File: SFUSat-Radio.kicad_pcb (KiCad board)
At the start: 4 copper layers, 95.9 x 90.2 mm, 282 parts, among them J1 PC104-8BIT, J10 TP_TH_150, J11 TP_TH_150, J12 SMA, J13 SMA, J14 SMA, J15 Conn_01x02, J16 SMA, J17 SMA, J18 SMA, J2 PC104PTH, J21 TP_TH_150, J22 TP_TH_150, J23 TP_TH_150, J24 TP_TH_150, J25 Conn_01x02, J3 PC104PTH, J4 PC104PTH, J400 SMA, J401 TP_TH_150, J402 TP_TH_150, J404 TP_TH_150, J405 TP_TH_150, J406 TP_TH_150, J5 PC104PTH, J500 SMA, J501 TP_TH_150, J502 TP_TH_150, J504 TP_TH_150, J505 TP_TH_150, J506 TP_TH_150, J6 SMA, J7 TP_TH_150, J8 TP_TH_150, J9 TP_TH_150, P1 3pin-DC-power, U1 SINGLE_0402, U10 TPS799, U100 CC1101-Q1, U101 0433BM15A0001, U11 SINGLE_0402, U110 CC1101-Q1, U111 0915BM15A0001E, U12 CONN_02X05_SHRD, U13 CONN_02X05_SHRD, U14 2N7002DW, U15 TPS62175DQCR, U16 TPS71750DSER, U17 74LVC1G14SE-7, U2 SKY13345-368LF, U3 CD4555BPWR, U4 LMS3635AQRNLRQ1, U400 SINGLE_0402, U401 LMV358, U402 RF6886, U420 2N7002DW, U5 MML09211H, U500 SINGLE_0402, U501 LMV358, U502 RF6886, U6 SINGLE_0402, U600 STLM75, U610 STLM75, U7 SKY13372-467LF, U8 SINGLE_0402, U9 TLV702, X100 NX3225GA, X110 NX3225GA

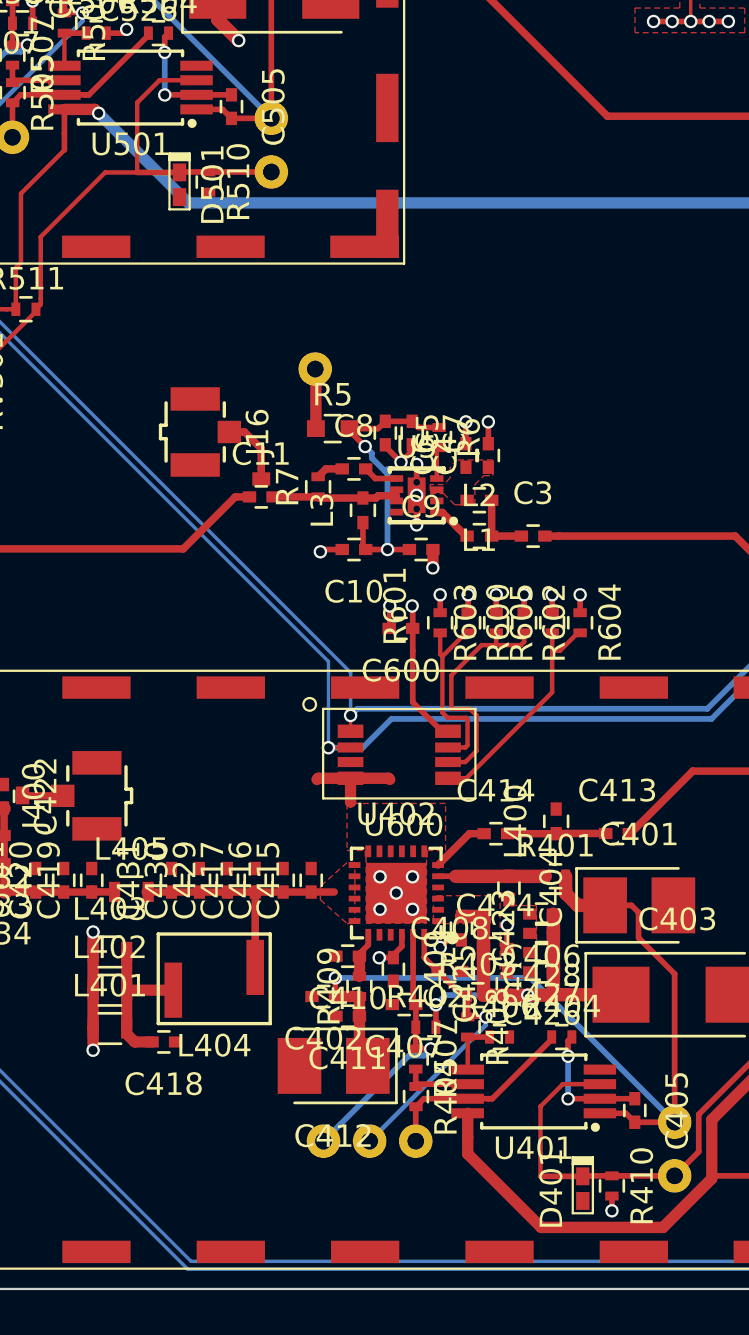
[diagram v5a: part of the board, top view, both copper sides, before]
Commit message: modified proposed pot schematic
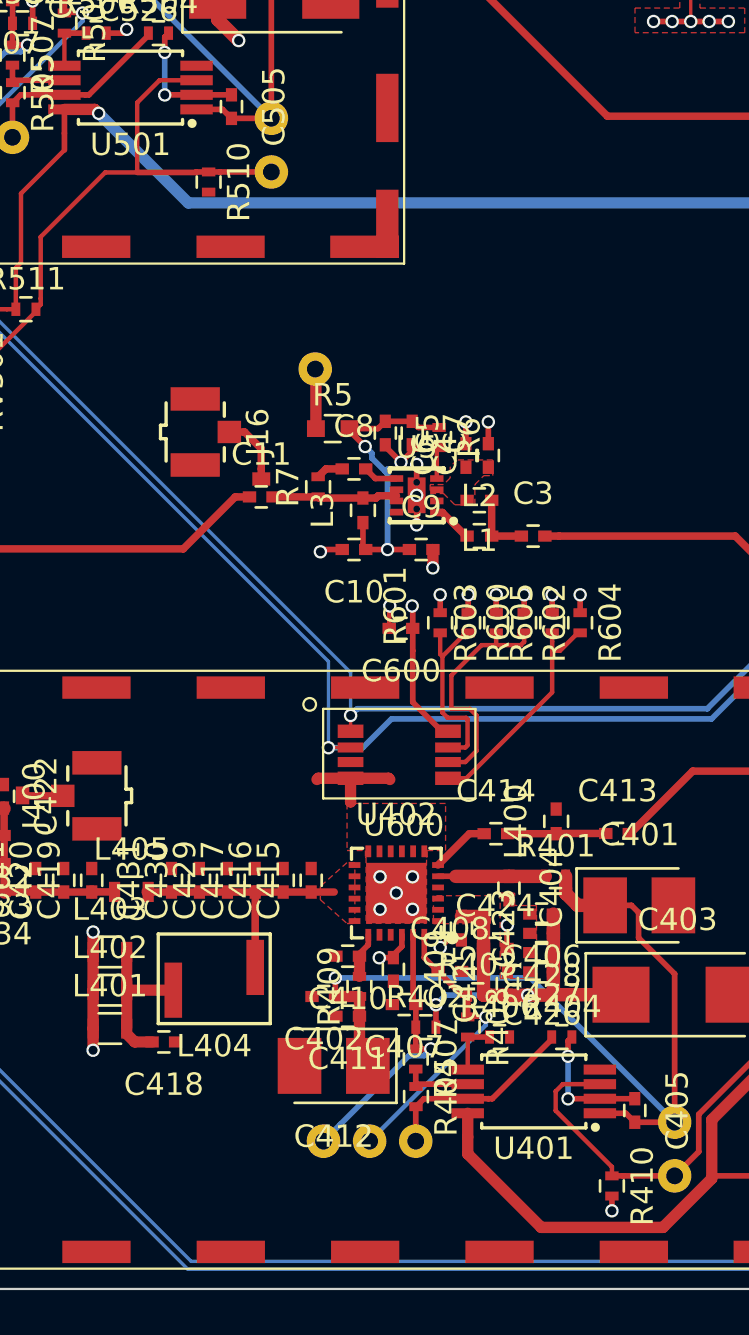
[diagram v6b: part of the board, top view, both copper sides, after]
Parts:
- removed D401, D501: PESD5Zx, SFUSat:PESD57zx
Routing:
- net /PA_LB/GAIN: track 37.8 -> 35.3 mm
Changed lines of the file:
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@@
     (thickness 1.6)
     (drawings 26)
-    (tracks 1615)
+    (tracks 1613)
     (zones 0)
-    (modules 282)
+    (modules 280)
     (nets 205)
   )
@@
       (net 1 GND))
   )
-  (module SFUSat:PESD57zx (layer F.Cu)
-    (at 142.86 99.19 270)
-    (fp_text reference D501 (at 0 -1.5 270) (layer F.SilkS)
-      (effects (font (size 1 1) (thickness 0.15)))
-    )
-    (fp_text value PESD5Zx (at 0 1.5 270) (layer F.Fab)
-      (effects (font (size 1 1) (thickness 0.15)))
-    )
-    (fp_line (start -1.6 -0.65) (end 1.3 -0.65) (layer F.CrtYd) (width 0.1))
-    (fp_line (start 1.3 -0.65) (end 1.3 0.65) (layer F.CrtYd) (width 0.1))
-    (fp_line (start 1.3 0.65) (end -1.6 0.65) (layer F.CrtYd) (width 0.1))
-    (fp_line (start -1.6 0.65) (end -1.6 -0.65) (layer F.CrtYd) (width 0.1))
-    (fp_text user REF** (at 0 -1.5 270) (layer F.Fab)
-      (effects (font (size 1 1) (thickness 0.15)))
-    )
-    (fp_line (start -1.4 -0.45) (end -1.4 0.45) (layer F.SilkS) (width 0.1))
-    (fp_line (start -1.2 -0.45) (end -1.2 0.45) (layer F.SilkS) (width 0.1))
-    (fp_line (start -1.1 -0.45) (end -1.4 -0.45) (layer F.SilkS) (width 0.1))
-    (fp_line (start -1.3 -0.45) (end -1.3 0.45) (layer F.SilkS) (width 0.1))
-    (fp_line (start -1.4 0.45) (end -1.1 0.45) (layer F.SilkS) (width 0.1))
-    (fp_line (start -1.1 -0.45) (end 1.1 -0.45) (layer F.SilkS) (width 0.1))
-    (fp_line (start 1.1 -0.45) (end 1.1 0.45) (layer F.SilkS) (width 0.1))
-    (fp_line (start 1.1 0.45) (end -1.1 0.45) (layer F.SilkS) (width 0.1))
-    (fp_line (start -1.1 0.45) (end -1.1 -0.45) (layer F.SilkS) (width 0.1))
-    (fp_line (start -0.15 0.225) (end -0.05 0.225) (layer F.Fab) (width 0.1))
-    (fp_line (start -1 -0.35) (end 1 -0.35) (layer F.Fab) (width 0.1))
-    (fp_line (start 1 -0.35) (end 1 0.35) (layer F.Fab) (width 0.1))
-    (fp_line (start 1 0.35) (end -1 0.35) (layer F.Fab) (width 0.1))
-    (fp_line (start -1 0.35) (end -1 -0.35) (layer F.Fab) (width 0.1))
-    (fp_line (start -0.15 -0.225) (end -0.15 0.225) (layer F.Fab) (width 0.1))
-    (fp_line (start 0.125 -0.225) (end 0.125 0.225) (layer F.Fab) (width 0.1))
-    (fp_line (start 0.125 0.225) (end -0.1 0) (layer F.Fab) (width 0.1))
-    (fp_line (start -0.1 0) (end 0.125 -0.225) (layer F.Fab) (width 0.1))
-    (pad 1 smd rect (at -0.55 0 270) (size 0.8 0.6) (layers F.Cu F.Paste F.Mask)
-      (net 106 /PA_UB/GAIN))
-    (pad 2 smd rect (at 0.55 0 270) (size 0.8 0.6) (layers F.Cu F.Paste F.Mask)
-      (net 1 GND))
-  )
-  (module SFUSat:PESD57zx (layer F.Cu)
-    (at 160.87 144.02 270)
-    (fp_text reference D401 (at 0 1.39 270) (layer F.SilkS)
-      (effects (font (size 1 1) (thickness 0.15)))
-    )
-    (fp_text value PESD5Zx (at 0 1.5 270) (layer F.Fab)
-      (effects (font (size 1 1) (thickness 0.15)))
-    )
-    (fp_line (start -1.6 -0.65) (end 1.3 -0.65) (layer F.CrtYd) (width 0.1))
-    (fp_line (start 1.3 -0.65) (end 1.3 0.65) (layer F.CrtYd) (width 0.1))
-    (fp_line (start 1.3 0.65) (end -1.6 0.65) (layer F.CrtYd) (width 0.1))
-    (fp_line (start -1.6 0.65) (end -1.6 -0.65) (layer F.CrtYd) (width 0.1))
-    (fp_text user REF** (at 0 -1.5 270) (layer F.Fab)
-      (effects (font (size 1 1) (thickness 0.15)))
-    )
-    (fp_line (start -1.4 -0.45) (end -1.4 0.45) (layer F.SilkS) (width 0.1))
-    (fp_line (start -1.2 -0.45) (end -1.2 0.45) (layer F.SilkS) (width 0.1))
-    (fp_line (start -1.1 -0.45) (end -1.4 -0.45) (layer F.SilkS) (width 0.1))
-    (fp_line (start -1.3 -0.45) (end -1.3 0.45) (layer F.SilkS) (width 0.1))
-    (fp_line (start -1.4 0.45) (end -1.1 0.45) (layer F.SilkS) (width 0.1))
-    (fp_line (start -1.1 -0.45) (end 1.1 -0.45) (layer F.SilkS) (width 0.1))
-    (fp_line (start 1.1 -0.45) (end 1.1 0.45) (layer F.SilkS) (width 0.1))
-    (fp_line (start 1.1 0.45) (end -1.1 0.45) (layer F.SilkS) (width 0.1))
-    (fp_line (start -1.1 0.45) (end -1.1 -0.45) (layer F.SilkS) (width 0.1))
-    (fp_line (start -0.15 0.225) (end -0.05 0.225) (layer F.Fab) (width 0.1))
-    (fp_line (start -1 -0.35) (end 1 -0.35) (layer F.Fab) (width 0.1))
-    (fp_line (start 1 -0.35) (end 1 0.35) (layer F.Fab) (width 0.1))
-    (fp_line (start 1 0.35) (end -1 0.35) (layer F.Fab) (width 0.1))
-    (fp_line (start -1 0.35) (end -1 -0.35) (layer F.Fab) (width 0.1))
-    (fp_line (start -0.15 -0.225) (end -0.15 0.225) (layer F.Fab) (width 0.1))
-    (fp_line (start 0.125 -0.225) (end 0.125 0.225) (layer F.Fab) (width 0.1))
-    (fp_line (start 0.125 0.225) (end -0.1 0) (layer F.Fab) (width 0.1))
-    (fp_line (start -0.1 0) (end 0.125 -0.225) (layer F.Fab) (width 0.1))
-    (pad 1 smd rect (at -0.55 0 270) (size 0.8 0.6) (layers F.Cu F.Paste F.Mask)
-      (net 101 /PA_LB/GAIN))
-    (pad 2 smd rect (at 0.55 0 270) (size 0.8 0.6) (layers F.Cu F.Paste F.Mask)
-      (net 1 GND))
-  )
   (module SFUSat-res:R_0402 (layer F.Cu)
     (at 192 99.5)
@@
   (segment (start 190.25 144.404) (end 190.25 143.75) (width 0.254) (layer F.Cu) (net 100))
   (segment (start 191.650001 146.529999) (end 191.55 146.63) (width 0.2) (layer F.Cu) (net 100))
+  (segment (start 159.976998 139.355) (end 159.657599 139.674399) (width 0.2) (layer F.Cu) (net 101))
+  (segment (start 159.657599 139.674399) (end 159.657599 140.537599) (width 0.2) (layer F.Cu) (net 101))
+  (segment (start 159.657599 140.537599) (end 162.17 143.05) (width 0.2) (layer F.Cu) (net 101))
+  (segment (start 162.17 143.05) (end 162.17 143.45) (width 0.2) (layer F.Cu) (net 101))
   (segment (start 179 131.5) (end 183.35 131.5) (width 0.2) (layer F.Cu) (net 101))
   (segment (start 183.35 131.5) (end 184 132.15) (width 0.2) (layer F.Cu) (net 101))
@@
   (segment (start 162.67 143.45) (end 164.97 143.45) (width 0.254) (layer F.Cu) (net 101))
   (segment (start 161.63 139.355) (end 159.976998 139.355) (width 0.2) (layer F.Cu) (net 101))
-  (segment (start 159.976998 139.355) (end 158.98 140.351998) (width 0.2) (layer F.Cu) (net 101))
-  (segment (start 158.98 140.351998) (end 158.98 142.47) (width 0.2) (layer F.Cu) (net 101))
-  (segment (start 158.98 142.47) (end 158.98 143.47) (width 0.2) (layer F.Cu) (net 101))
-  (segment (start 158.98 143.47) (end 160.87 143.47) (width 0.254) (layer F.Cu) (net 101))
-  (segment (start 162.17 143.45) (end 160.89 143.45) (width 0.254) (layer F.Cu) (net 101))
-  (segment (start 160.89 143.45) (end 160.87 143.47) (width 0.254) (layer F.Cu) (net 101))
   (segment (start 184.25 142.07) (end 183.23 142.07) (width 0.254) (layer F.Cu) (net 102))
   (segment (start 183.23 142.07) (end 182.75 142.55) (width 0.254) (layer F.Cu) (net 102))
@@
   (segment (start 185.95 144.317429) (end 186.596 143.671429) (width 0.254) (layer F.Cu) (net 105))
   (segment (start 186.596 143.671429) (end 187.25 143.671429) (width 0.254) (layer F.Cu) (net 105))
+  (segment (start 144.16 98.62) (end 143.606 98.62) (width 0.254) (layer F.Cu) (net 106))
+  (segment (start 143.606 98.62) (end 143.586 98.64) (width 0.254) (layer F.Cu) (net 106))
+  (segment (start 143.586 98.64) (end 140.97 98.64) (width 0.254) (layer F.Cu) (net 106))
   (segment (start 136.45 104.75) (end 136.45 104.85) (width 0.2) (layer F.Cu) (net 106))
   (segment (start 136.45 104.85) (end 133.32 107.98) (width 0.2) (layer F.Cu) (net 106))
@@
   (segment (start 140.97 95.521998) (end 140.97 97.64) (width 0.2) (layer F.Cu) (net 106))
   (segment (start 140.97 97.64) (end 140.97 98.64) (width 0.2) (layer F.Cu) (net 106))
-  (segment (start 140.97 98.64) (end 142.86 98.64) (width 0.254) (layer F.Cu) (net 106))
-  (segment (start 144.16 98.62) (end 142.88 98.62) (width 0.254) (layer F.Cu) (net 106))
-  (segment (start 142.88 98.62) (end 142.86 98.64) (width 0.254) (layer F.Cu) (net 106))
   (segment (start 195.69 98.97) (end 196.877001 100.157001) (width 0.254) (layer B.Cu) (net 107))
   (segment (start 196.877001 100.157001) (end 196.877001 102.245759) (width 0.254) (layer B.Cu) (net 107))

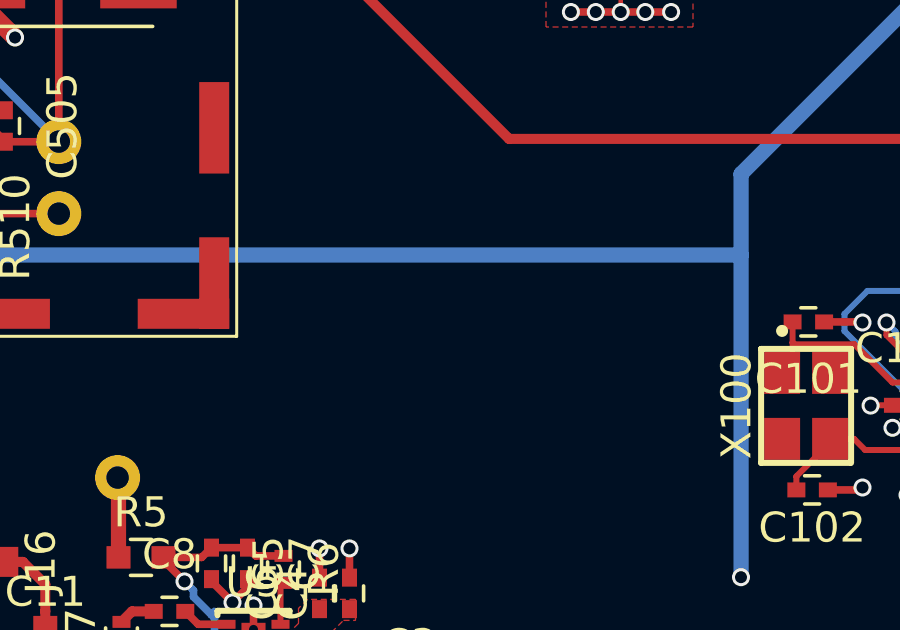
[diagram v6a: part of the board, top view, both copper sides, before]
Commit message: added antenna connector keepout
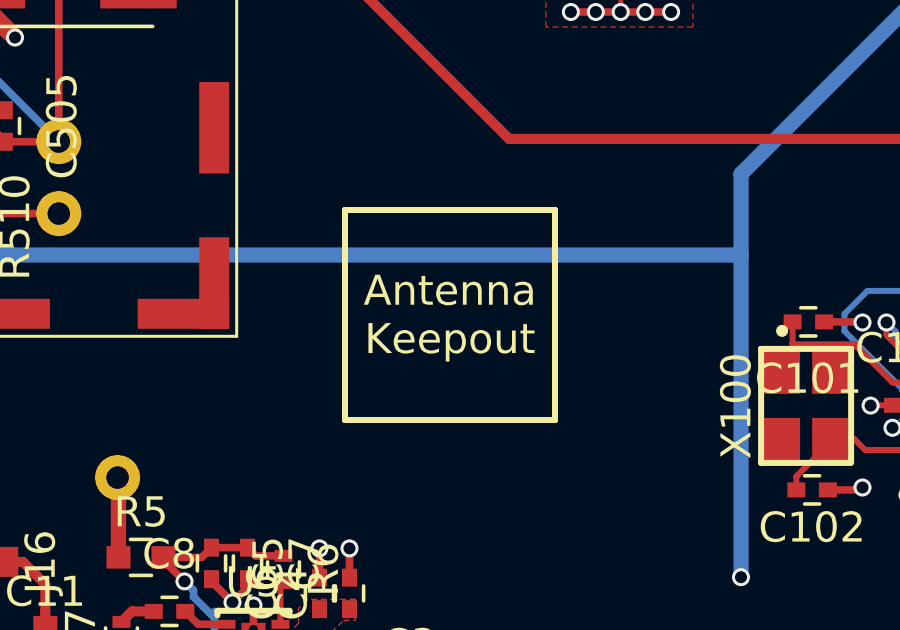
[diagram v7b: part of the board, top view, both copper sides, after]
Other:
- board text added: "Antenna Keepout"
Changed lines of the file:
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@@
     (area 112.449999 58.279999 208.440001 148.550001)
     (thickness 1.6)
-    (drawings 26)
+    (drawings 31)
     (tracks 1613)
     (zones 0)
@@
       (net 181 /VIN))
   )
+  (gr_line (start 156.5 98.5) (end 156.5 105.5) (layer F.SilkS) (width 0.2))
+  (gr_line (start 163.5 98.5) (end 156.5 98.5) (layer F.SilkS) (width 0.2))
+  (gr_line (start 163.5 105.5) (end 163.5 98.5) (layer F.SilkS) (width 0.2))
+  (gr_line (start 163.5 105.5) (end 156.5 105.5) (layer F.SilkS) (width 0.2))
+  (gr_text "Antenna\nKeepout" (at 160 102) (layer F.SilkS)
+    (effects (font (size 1 1) (thickness 0.15)))
+  )
   (gr_text GND (at 154.01 61.72 180) (layer F.SilkS)

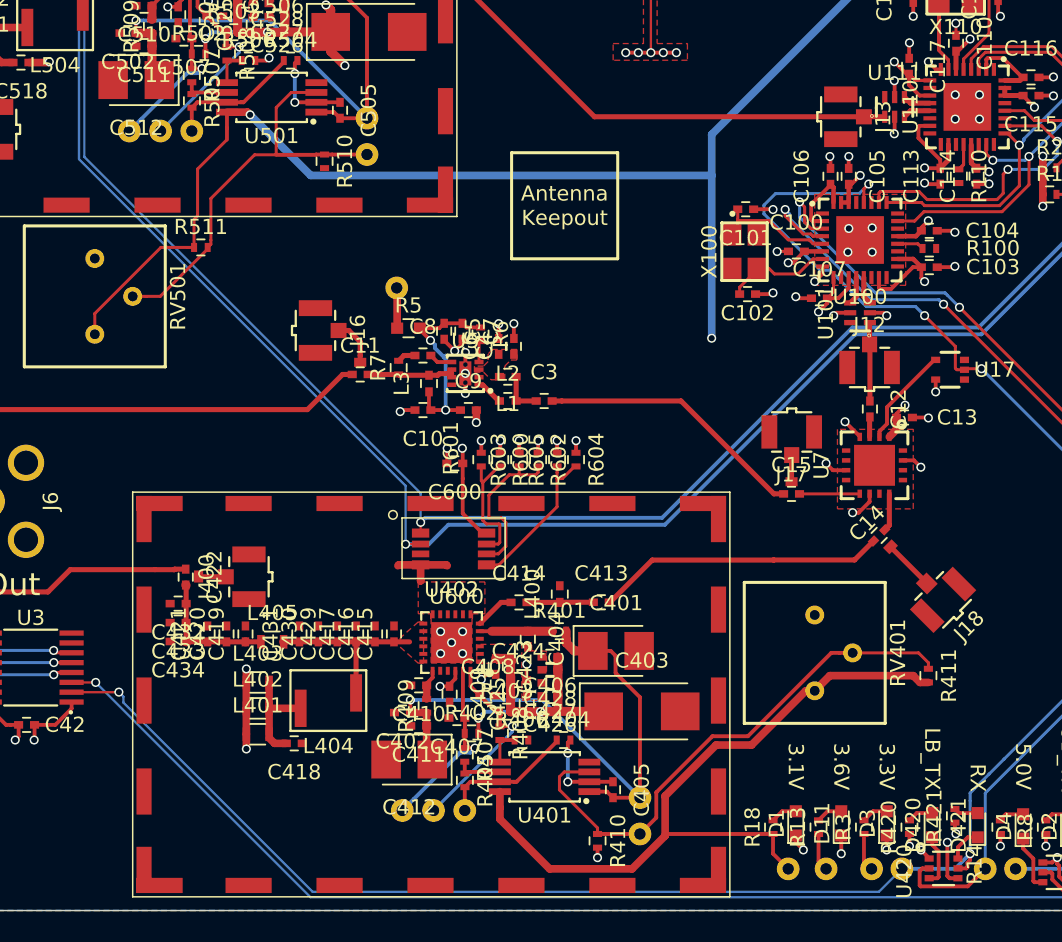
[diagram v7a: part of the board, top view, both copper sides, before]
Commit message: modified gain control circuit in following issue #54
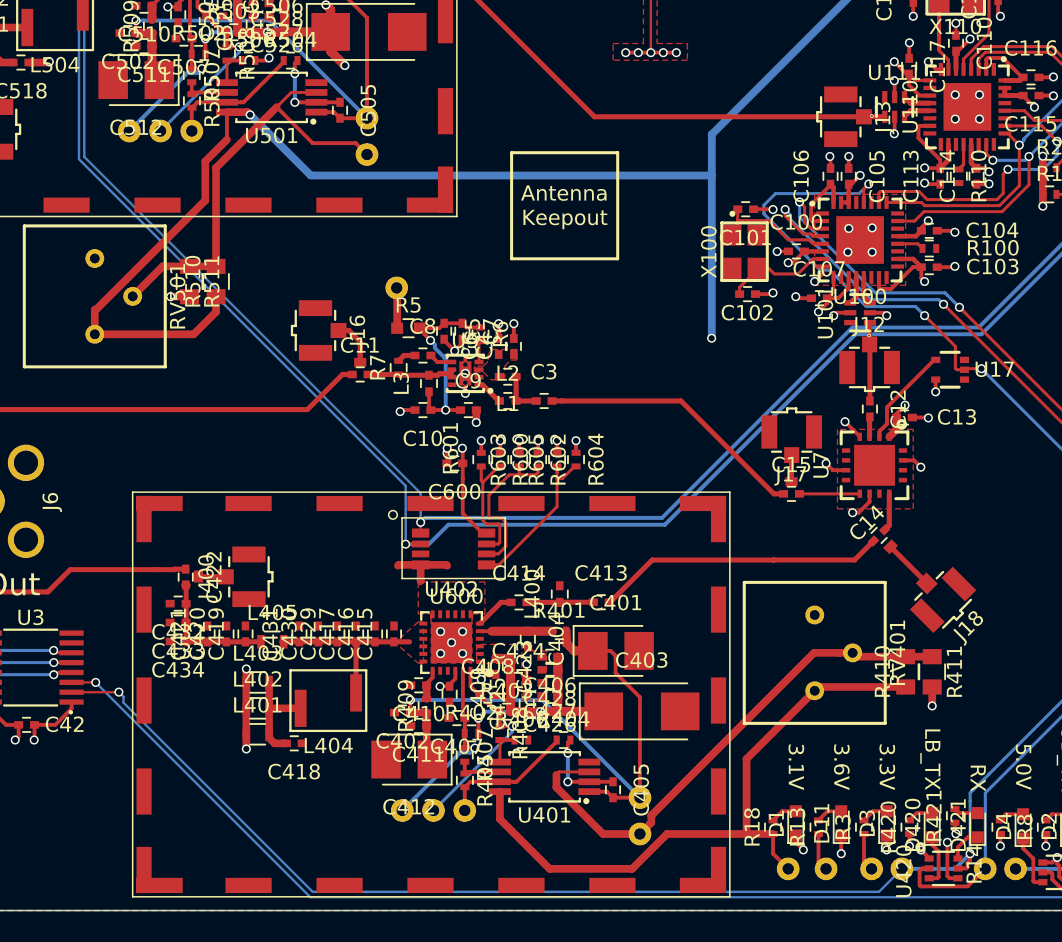
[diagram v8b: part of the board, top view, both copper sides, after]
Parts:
- C405, C505: value 0.1uF -> 0.33uF
- R410, R510: value 1K -> 100k; footprint SFUSat:R_0402 -> SFUSat-res:R_0805
- R411, R511: footprint SFUSat:R_0402 -> SFUSat-res:R_0805
- moved R410 23.2 mm to (182.5, 132.8), turned to 90 degrees
- moved R510 10.7 mm to (137.0, 107.0), turned to 90 degrees
- moved R511 2.37 mm to (135.2, 107.0), turned to 270 degrees
- moved R411 0.35 mm to (184.2, 132.8), turned to 270 degrees
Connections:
- R410 pad 1: /PA_LB/GAIN -> /3V1
- R410 pad 2: GND -> /PA_LB/GAIN
- R411 pad 1: /3V1 -> /PA_LB/GAIN
- R411 pad 2: /PA_LB/GAIN -> GND
- R510 pad 1: /PA_UB/GAIN -> /3V1
- R510 pad 2: GND -> /PA_UB/GAIN
- R511 pad 1: /3V1 -> /PA_UB/GAIN
- R511 pad 2: /PA_UB/GAIN -> GND
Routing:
- net /3V1: track 175.6 -> 178.3 mm
- net GND: track 124.1 -> 126.0 mm, vias 105 -> 106
- net /PA_UB/GAIN: track 27.4 -> 28.8 mm
- net /PA_LB/GAIN: track 35.3 -> 34.5 mm
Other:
- net class Default: clearance 0.1524 -> 0.2
- net class Power: clearance 0.1524 -> 0.2
- rule trace_clearance: 0.1524 -> 0.2
